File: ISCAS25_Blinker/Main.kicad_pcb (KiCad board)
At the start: 2 copper layers, 82.9 x 66.9 mm, 6 parts

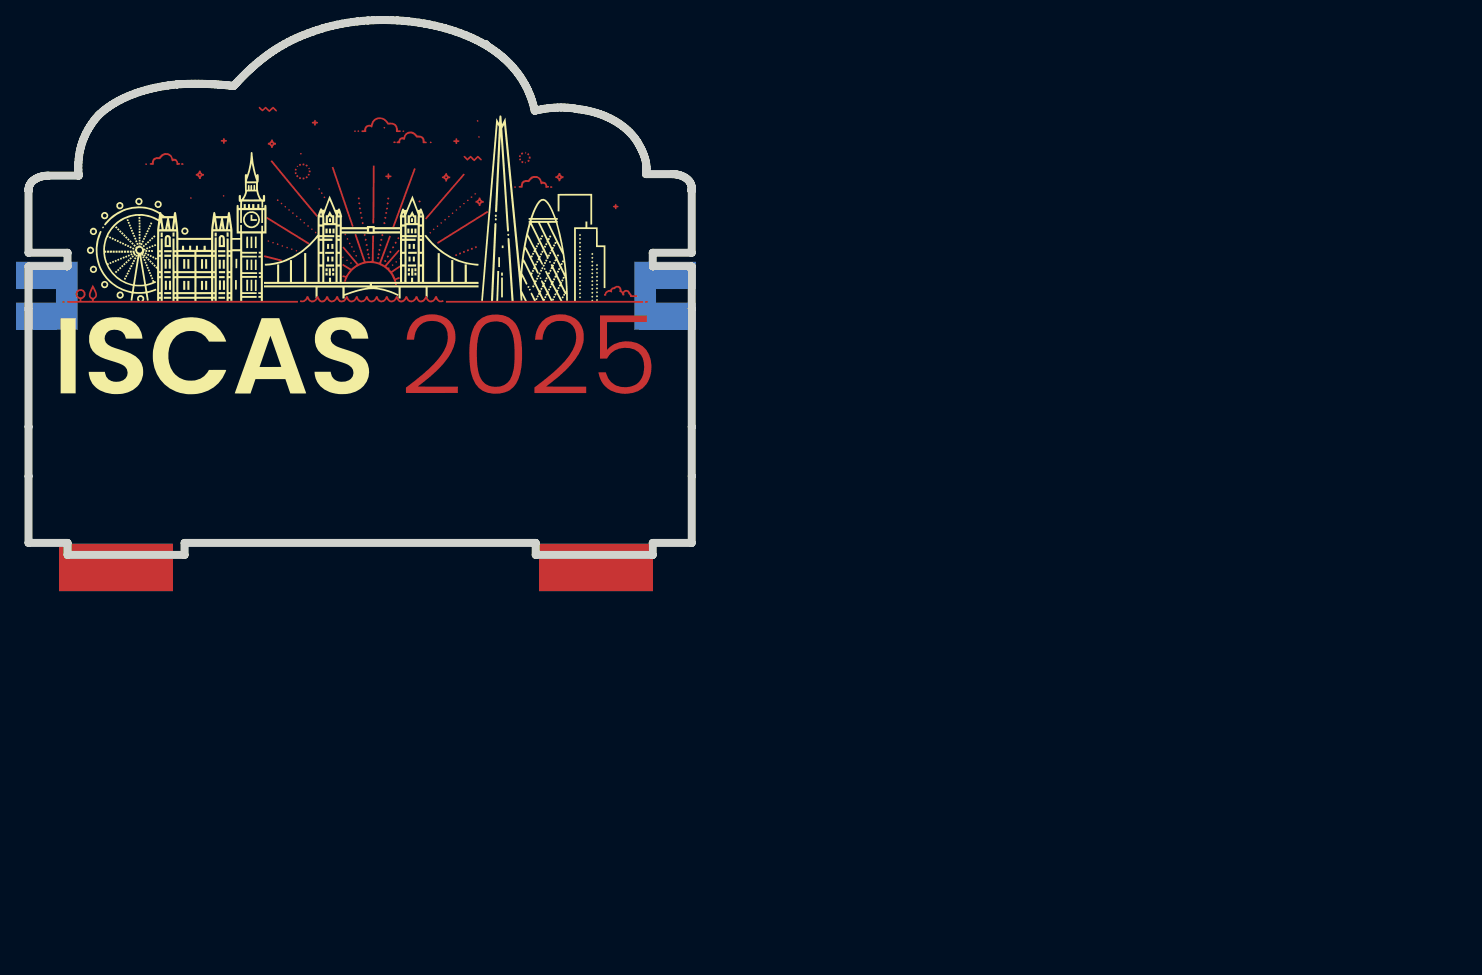
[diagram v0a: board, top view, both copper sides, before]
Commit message: Schematic done
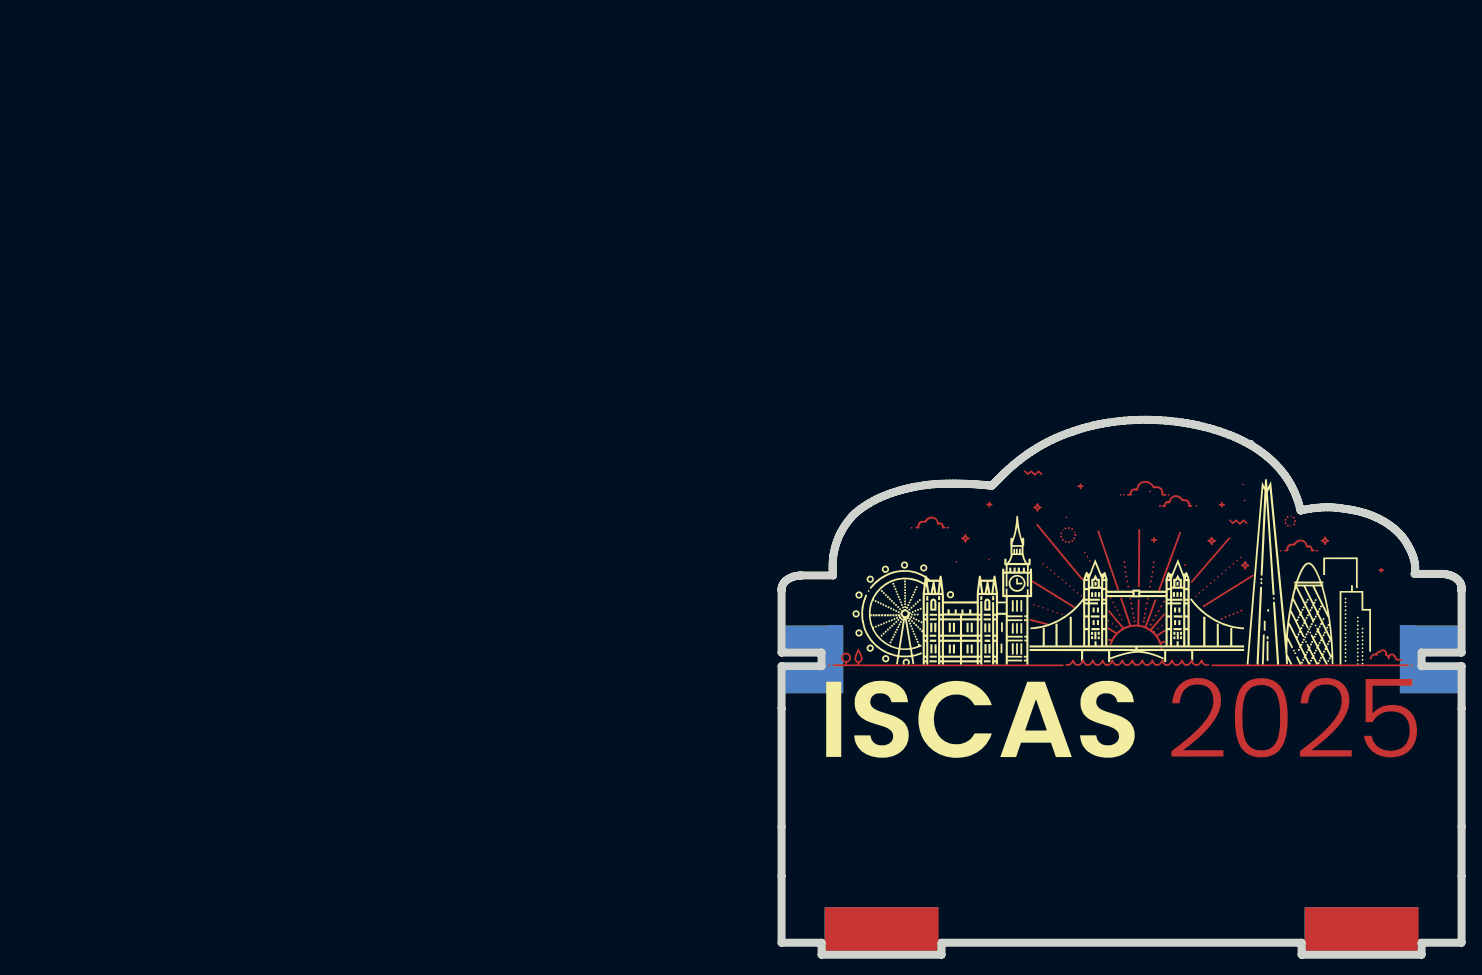
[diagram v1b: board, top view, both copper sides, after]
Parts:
- removed the ? at (0.00, 0.00) (x5)
- added ? (x4): , Graphics, F.Cu at (103.2, 60.9)
- added ?: , Graphics, B.Cu at (103.2, 60.9)
- ?: moved to F.Cu
- moved ? 119.8 mm to (103.2, 60.9)
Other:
- board size 82.9 x 66.9 mm -> 85 x 66.9 mm
